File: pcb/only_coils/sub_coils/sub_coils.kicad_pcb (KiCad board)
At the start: 4 copper layers, 70 x 50 mm, 8 parts, among them J2 Conn_01x06_Pin, J4 Conn_01x03_Pin

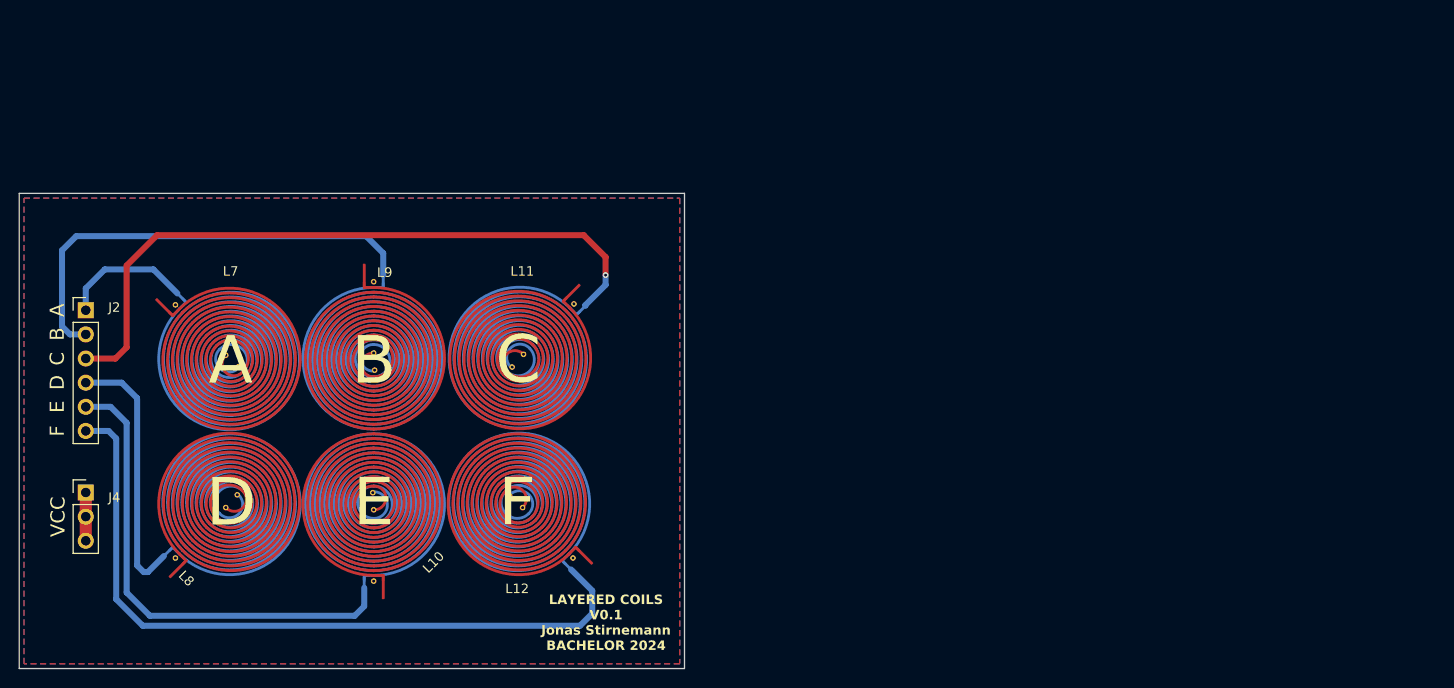
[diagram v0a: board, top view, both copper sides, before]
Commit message: Added second pcb
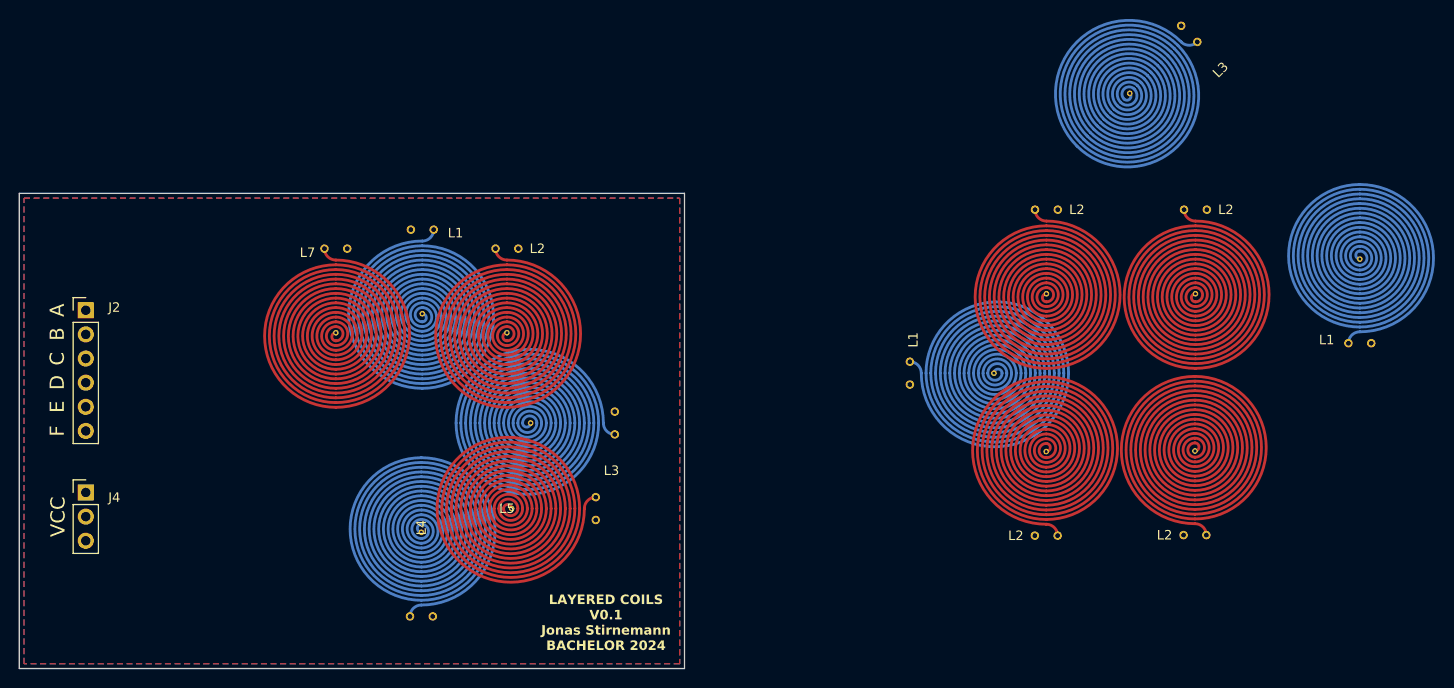
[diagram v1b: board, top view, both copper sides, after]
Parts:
- removed L10, L11, L12, L8, L9: coil_4_layers, single_coils:4layer_coil
- added L1: sub_coil, sub_coils:sub_coil, F.Cu at (169.8, 53.8)
- added L1: sub_coil, sub_coils:sub_coil, F.Cu at (207.8, 41.2)
- added L1: sub_coil, sub_coils:sub_coil, F.Cu at (109.1, 48.0)
- added L2: top_coil, sub_coils:top_coil, F.Cu at (190.4, 45.9)
- added L2: top_coil, sub_coils:top_coil, F.Cu at (174.8, 45.9)
- added L2: top_coil, sub_coils:top_coil, F.Cu at (174.8, 61.5)
- added L2: top_coil, sub_coils:top_coil, F.Cu at (190.4, 61.4)
- added L2: top_coil, sub_coils:top_coil, F.Cu at (118.0, 50.0)
- added L3: sub_coil, sub_coils:sub_coil, F.Cu at (183.2, 24.7)
- added L3: sub_coil, sub_coils:sub_coil, F.Cu at (120.0, 59.0)
- added L4: sub_coil, sub_coils:sub_coil, F.Cu at (109.0, 70.0)
- added L5: top_coil, sub_coils:top_coil, F.Cu at (118.0, 68.0)
- L7: value coil_4_layers -> top_coil; footprint single_coils:4layer_coil -> sub_coils:top_coil
- moved L7 11.3 mm to (100.0, 50.0), turned to 90 degrees
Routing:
- net /F: track 77.8 -> 0.00 mm
- net /C: track 72.1 -> 0.00 mm, vias 1 -> 0
- net /E: track 51.2 -> 0.00 mm
- net /B: track 48.3 -> 0.00 mm
- net /D: track 27.5 -> 0.00 mm
- net /A: track 13.8 -> 0.00 mm
- net VCC: track 5.08 -> 0.00 mm
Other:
- board text added: "LAYERED MODULE - 4 layer coils - 12 turns / layer - 11 mils traces - 10 mils gap"
- board text removed: "LAYERED MODULE - 4 layer coils - 12 turns / layer - 0.3 mils traces - 0.2 mils gap"

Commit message: Added small script for square coils
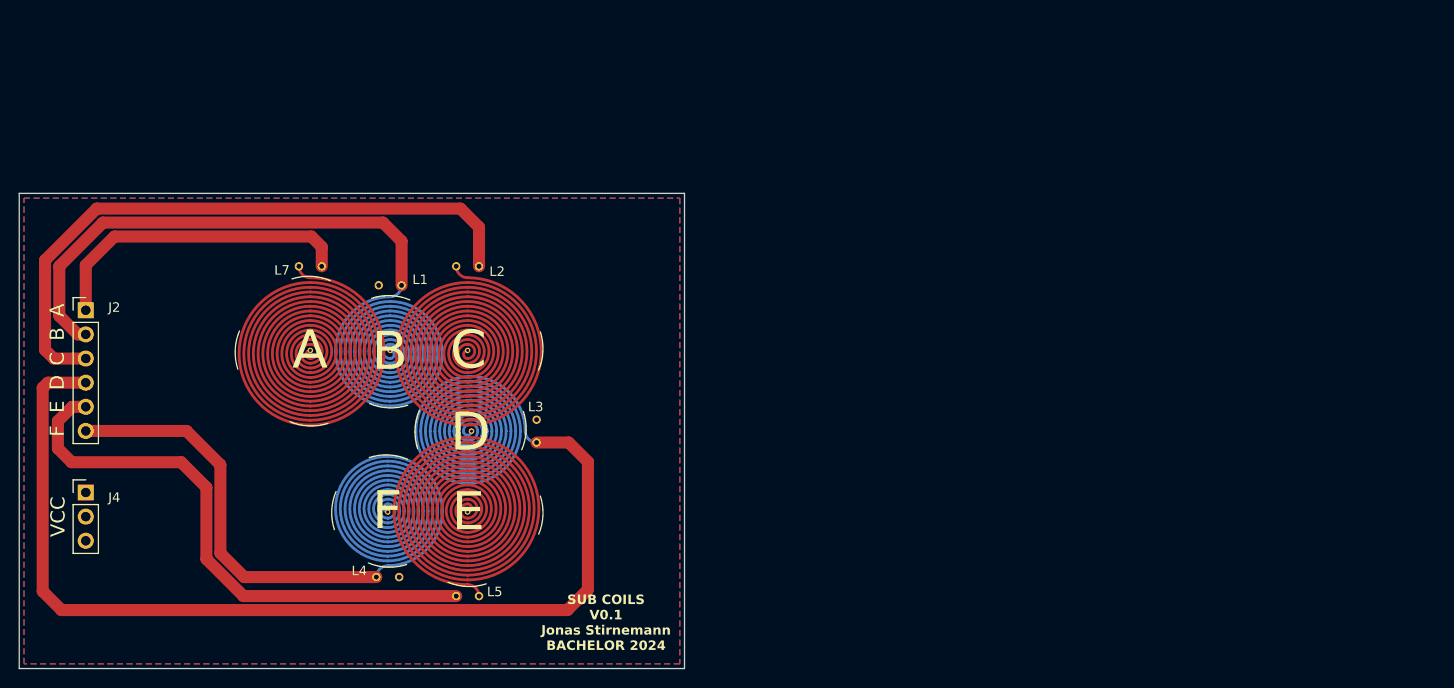
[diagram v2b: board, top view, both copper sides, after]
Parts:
- removed the L1 at (169.8, 53.8)
- removed the L1 at (207.8, 41.2)
- removed the L2 at (190.4, 45.9)
- removed the L2 at (174.8, 45.9)
- removed the L2 at (174.8, 61.5)
- removed the L2 at (190.4, 61.4)
- removed the L3 at (183.2, 24.7)
- L1, L3, L4: footprint sub_coils:sub_coil -> sub_coils:sub_coil_small_2
- moved L3 6.28 mm to (113.8, 59.9)
- moved L1 5.13 mm to (105.7, 51.9)
- moved L2 4.53 mm to (113.9, 51.9)
- moved L5 4.14 mm to (113.9, 67.9), turned to -90 degrees
- moved L4 4.13 mm to (105.5, 67.9)
- moved L7 3.27 mm to (97.3, 51.9)
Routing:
- net /D: track 0.00 -> 104.9 mm
- net /C: track 0.00 -> 66.9 mm
- net /E: track 0.00 -> 59.2 mm
- net /B: track 0.00 -> 52.2 mm
- net /F: track 0.00 -> 42.4 mm
- net /A: track 0.00 -> 33.3 mm
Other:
- board text added: "SUB COILS MODULE - 2 layer coils sandwiched with with subcoils - 0.3 mm traces - 0.2 mm gap"
- board text added: "SUB COILS V0.1 Jonas Stirnemann BACHELOR 2024"
- board text removed: "LAYERED COILS V0.1 Jonas Stirnemann BACHELOR 2024"
- board text removed: "LAYERED MODULE - 4 layer coils - 12 turns / layer - 11 mils traces - 10 mils gap"
